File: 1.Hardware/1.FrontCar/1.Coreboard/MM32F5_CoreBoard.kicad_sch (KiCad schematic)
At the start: 61 parts

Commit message: 增加CAN接口
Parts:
- added J? (x2): (no value), symbol Connector_Generic_MountingPin:Conn_01x02_MountingPin
- added R?: 0R, ErBW_s:R_0402, symbol Device:R_Small
- added R?: (no value), ErBW_s:R_0402, symbol Device:R_Small
- added SW? (x3): 3x4, ErBW_s:BUTTON_3x4, symbol Switch:SW_Push
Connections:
- net +3.3VA: now also R?.1; no longer C?.1, C?.1, C?.1, C?.1, C?.2, C?.2, C?.2, C?.2, C?.2, C?.2, C?.2, C?.2, C?.2, C?.2, C?.2, C?.2, C?.2, J?.1 (Pin_1), J?.10 (VCC), J?.12 (LEDA), R?.1, R?.1, R?.1, R?.1, R?.1, U?.108 (VDD), U?.121 (VDD), U?.13 (VDD), U?.131 (VDD), U?.144 (VDD), U?.17 (VDD), U?.3 (VCC), U?.3 (VCC), U?.39 (VDD), U?.5 (VOUT), U?.52 (VDD), U?.6 (VBAT), U?.62 (VDD), U?.72 (VDD), U?.8 (VDDIO), U?.84 (VDD), U?.95 (VDD)
- net CAN1_H: now also J?.2 (Pin_2)
- net CAN1_L: now also J?.1 (Pin_1)
- net CAN2_H: now also J?.2 (Pin_2)
- net CAN2_L: now also J?.1 (Pin_1)
- net ENCODER_A: now also SW?.1
- net ENCODER_B: now also SW?.1
- net GND: now also J?.MP (MountPin), J?.MP (MountPin), R?.2, SW?.2, SW?.2, SW?.2; no longer C?.1, U?.30 (VSSA), U?.31 (VREF-)
- net PG8 renamed KEY_CENTER
- net KEY_CENTER: now also SW?.1
- new net +3.3V: C?.1, C?.1, C?.1, C?.1, C?.2, C?.2, C?.2, C?.2, C?.2, C?.2, C?.2, C?.2, C?.2, C?.2, C?.2, C?.2, C?.2, J?.1 (Pin_1), J?.10 (VCC), J?.12 (LEDA), R?.1, R?.1, R?.1, R?.1, R?.1, R?.2, U?.108 (VDD), U?.121 (VDD), U?.13 (VDD), U?.131 (VDD), U?.144 (VDD), U?.17 (VDD), U?.3 (VCC), U?.3 (VCC), U?.39 (VDD), U?.5 (VOUT), U?.52 (VDD), U?.6 (VBAT), U?.62 (VDD), U?.72 (VDD), U?.8 (VDDIO), U?.84 (VDD), U?.95 (VDD)
- new net GNDA: C?.1, R?.1, U?.30 (VSSA), U?.31 (VREF-)
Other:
- note added: "BTB"
- note added: "KEY"
- note added: "PORTS"
- note removed: "SWD"
- moved on the sheet: C?, D?, J?, R?, U?

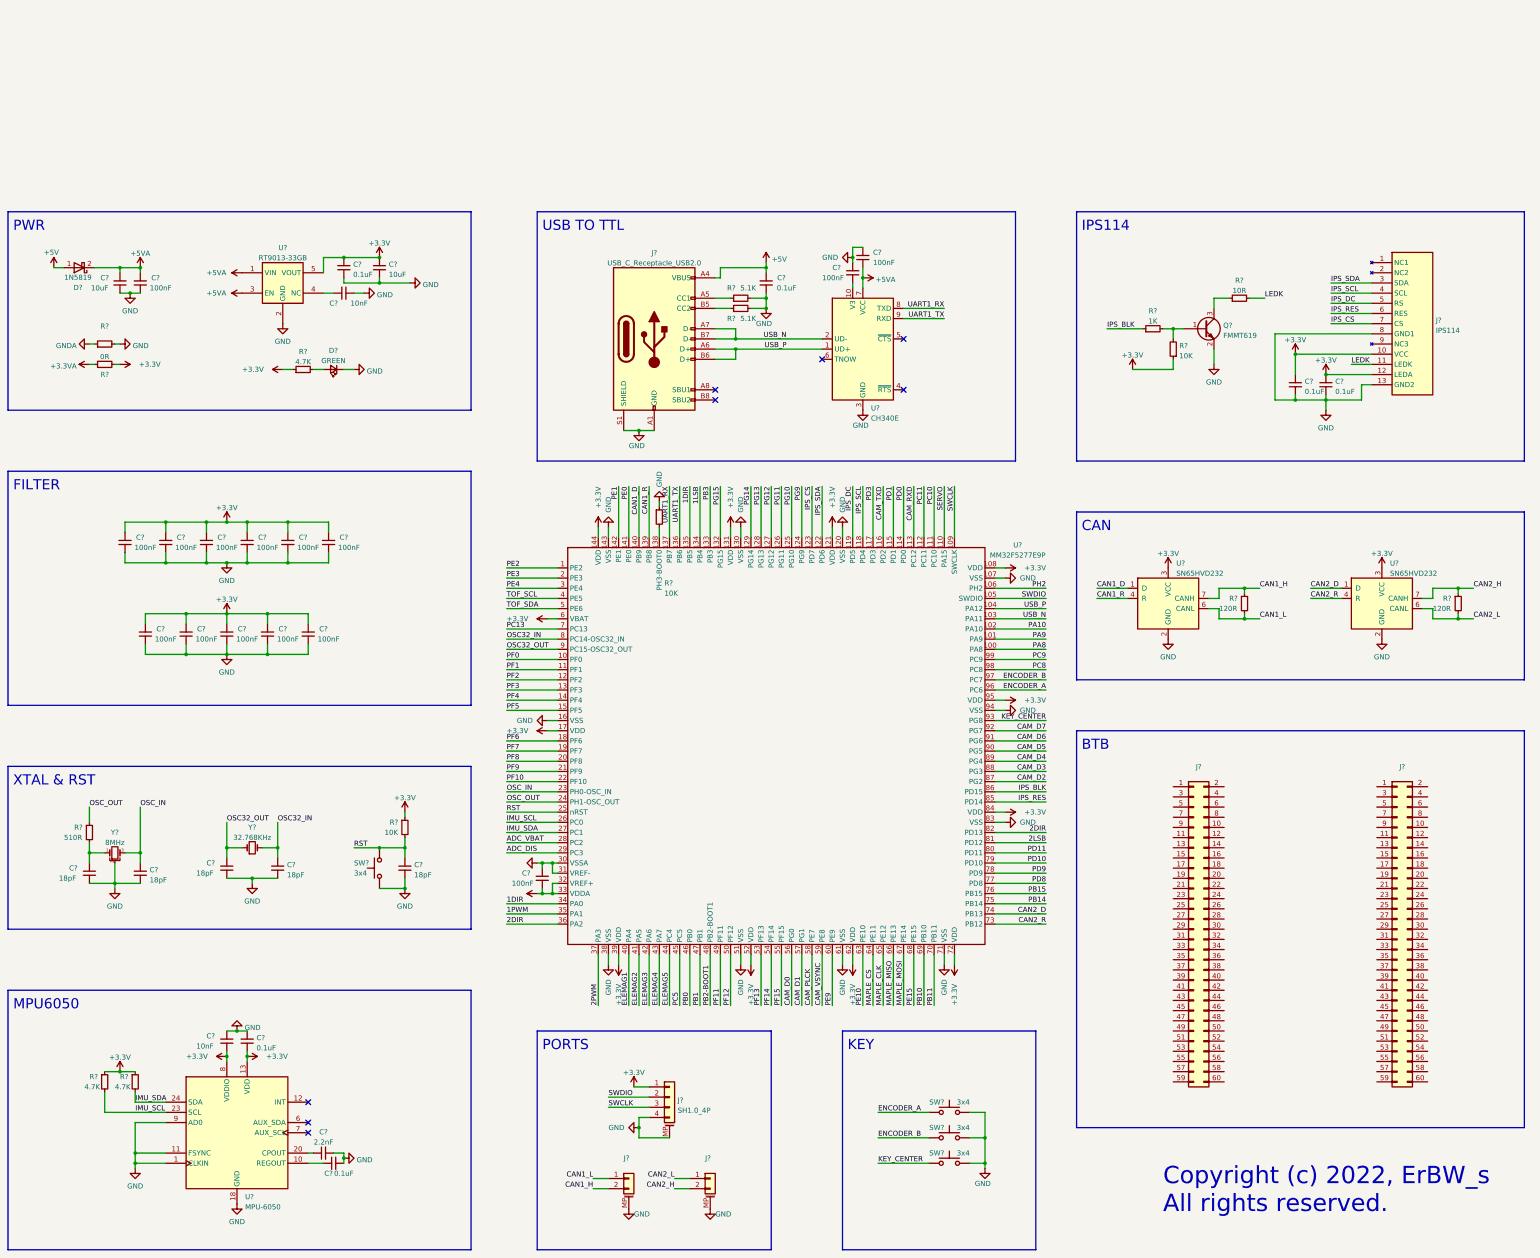
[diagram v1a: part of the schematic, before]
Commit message: 改用ch343p作为usb to ttl 芯片
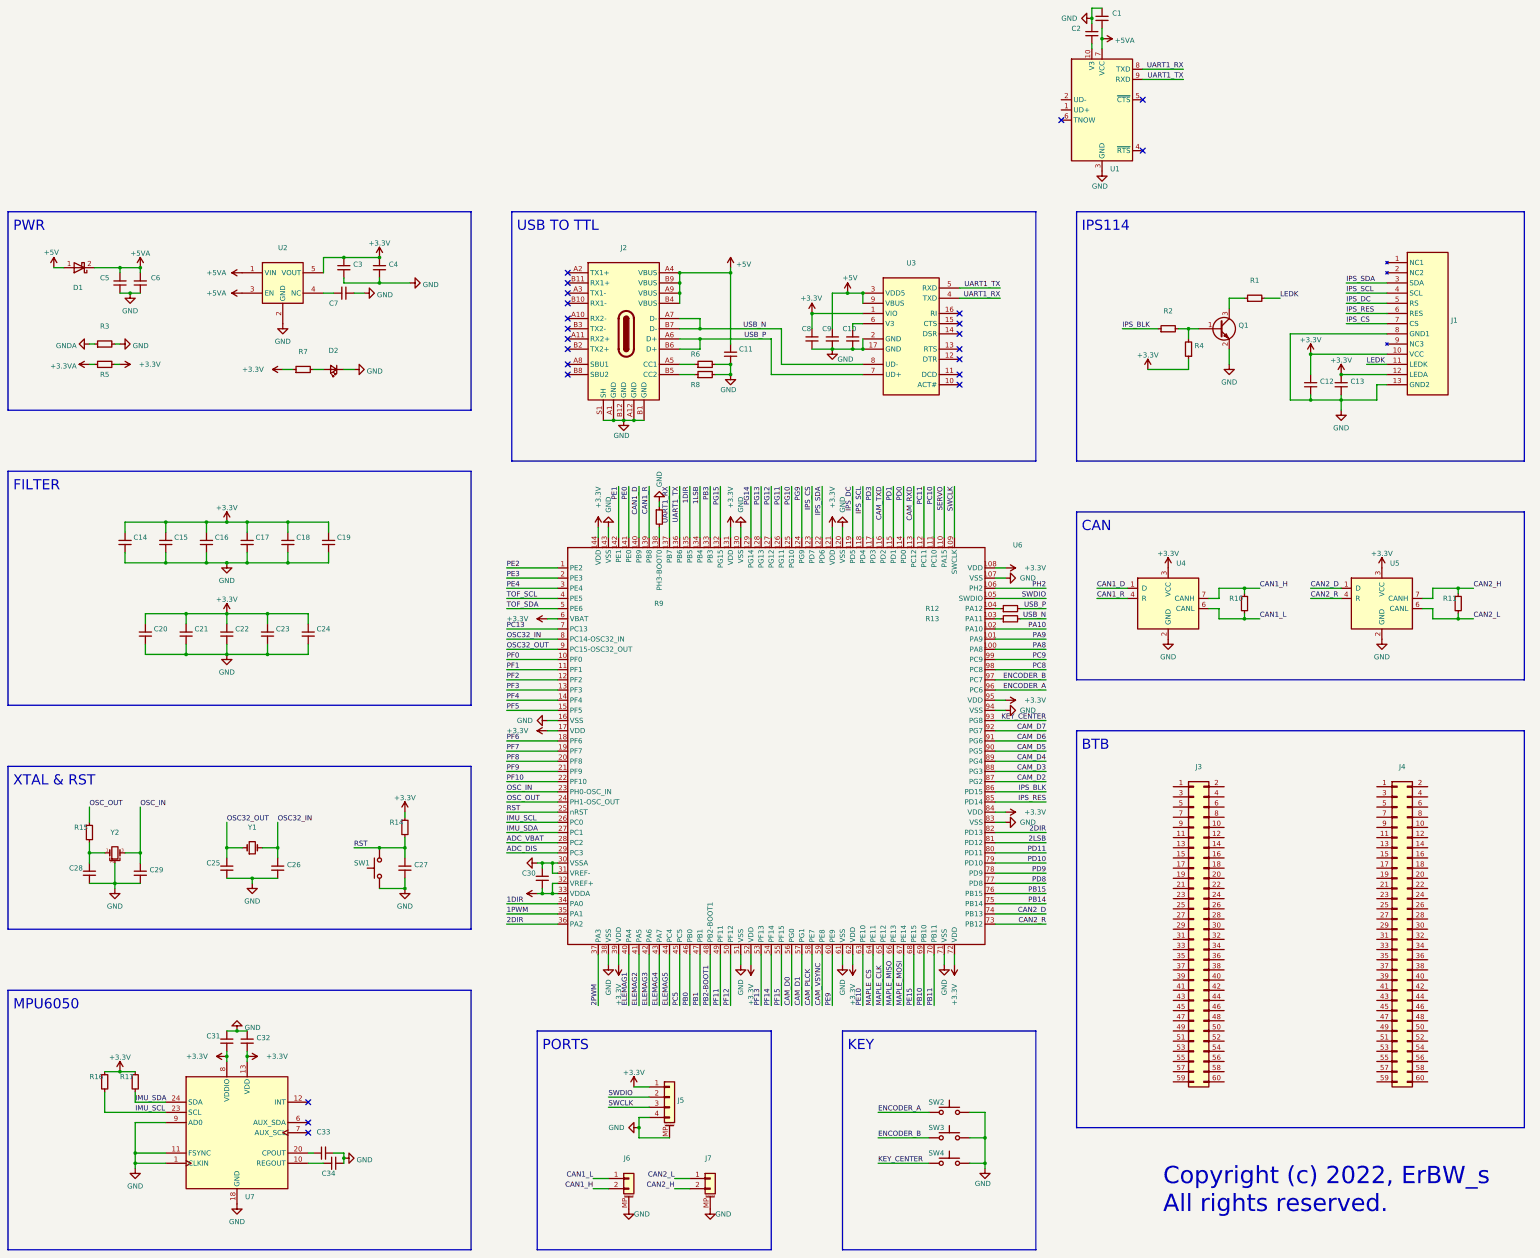
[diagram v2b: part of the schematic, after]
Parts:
- removed C?: 0.1uF, ErBW_s:C_0402, symbol Device:C_Small
- removed J?: USB_C_Receptacle_USB2.0, symbol Connector:USB_C_Receptacle_USB2.0
- removed R? (x2): 5.1K, ErBW_s:R_0402, symbol Device:R_Small
- added C10, C11, C8, C9: (no value), symbol Device:C_Small
- added J2: USB-Type-C, ErBW_s:USB-Type-C_SMD_16P, symbol ErBW_s:USB-Type-C
- added R12, R13, R6, R8: (no value), symbol Device:R_Small
- added U3: CH343P, Package_DFN_QFN:QFN-16-1EP_3x3mm_P0.5mm_EP1.7x1.7mm, symbol ErBW_s:CH343P
- C1, C14, C15, C16, C17, C18, C19, C2, C20, C21, C22, C23, C24, C30, C6: renamed from C?; value 100nF -> (none); footprint ErBW_s:C_0402 -> (none)
- C12, C13, C3, C32, C34: renamed from C?; value 0.1uF -> (none); footprint ErBW_s:C_0402 -> (none)
- C25, C26, C27, C28, C29: renamed from C?; value 18pF -> (none); footprint ErBW_s:C_0402 -> (none)
- C31, C7: renamed from C?; value 10nF -> (none); footprint ErBW_s:C_0402 -> (none)
- C33: renamed from C?; value 2.2nF -> (none); footprint ErBW_s:C_0402 -> (none)
- C4, C5: renamed from C?; value 10uF -> (none); footprint ErBW_s:C_0402 -> (none)
- D1: renamed from D?; value 1N5819 -> (none); footprint ErBW_s:SOD-323 -> (none)
- D2: renamed from D?; value GREEN -> (none); footprint ErBW_s:LED_0402 -> (none)
- J1: renamed from J?; value IPS114 -> (none); footprint ErBW_s:IPS114 -> (none)
- J5: renamed from J?; value SH1.0_4P -> (none); footprint Connector_JST:JST_SH_SM04B-SRSS-TB_1x04-1MP_P1.00mm_Horizontal -> (none)
- J6: renamed from J?; value (none) -> SH1.0_2P; footprint (none) -> Connector_JST:JST_SH_SM02B-SRSS-TB_1x02-1MP_P1.00mm_Horizontal
- Q1: renamed from Q?; value FMMT619 -> (none); footprint Package_TO_SOT_SMD:SOT-23 -> (none)
- R1: renamed from R?; value 10R -> (none); footprint ErBW_s:R_0402 -> (none)
- R10, R11: renamed from R?; value 120R -> (none); footprint ErBW_s:R_0402 -> (none)
- R14, R4, R9: renamed from R?; value 10K -> (none); footprint ErBW_s:R_0402 -> (none)
- R15: renamed from R?; value 510R -> (none); footprint ErBW_s:R_0402 -> (none)
- R16, R17, R7: renamed from R?; value 4.7K -> (none); footprint ErBW_s:R_0402 -> (none)
- R2: renamed from R?; value 1K -> (none); footprint ErBW_s:R_0402 -> (none)
- R3: renamed from R?; footprint ErBW_s:R_0402 -> (none)
- R5: renamed from R?; value 0R -> (none); footprint ErBW_s:R_0402 -> (none)
- SW1, SW2, SW3, SW4: renamed from SW?; value 3x4 -> (none); footprint ErBW_s:BUTTON_3x4 -> (none)
- U1: renamed from U?; value CH340E -> (none); footprint Package_SO:MSOP-10_3x3mm_P0.5mm -> (none)
- U2: renamed from U?; value RT9013-33GB -> (none); footprint Package_TO_SOT_SMD:SOT-23-5 -> (none)
- U4, U5: renamed from U?; value SN65HVD232 -> (none); footprint Package_SO:SOIC-8_3.9x4.9mm_P1.27mm -> (none)
- U6: renamed from U?; value MM32F5277E9P -> (none); footprint Package_QFP:LQFP-144_20x20mm_P0.5mm -> (none)
- U7: renamed from U?; value MPU-6050 -> (none); footprint Sensor_Motion:InvenSense_QFN-24_4x4mm_P0.5mm -> (none)
- Y1: renamed from Y?; value 32.768KHz -> (none); footprint ErBW_s:Crystal_SMD_3215_FC-135_2P -> (none)
- Y2: renamed from Y?; value 8MHz -> (none); footprint ErBW_s:Crystal_SMD_3213_3P -> (none)
- gave numbers to parts that had none: 3
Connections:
- net +3.3V: now also C8.1, U3.1 (VIO)
- net +5V: now also C11.2, C9.1, J2.A4 (VBUS), J2.A9 (VBUS), J2.B4 (VBUS), J2.B9 (VBUS), U3.3 (VDD5), U3.9 (VBUS)
- net GND: now also C10.2, C11.1, C8.2, C9.2, J2.A1 (GND), J2.A12 (GND), J2.B1 (GND), J2.B12 (GND), J2.S1 (SH), R6.2, R8.2, U3.17 (GND), U3.2 (GND)
- net UART1_RX: now also U3.4 (TXD)
- net UART1_TX: now also U3.5 (RXD)
- net USB_N: now also J2.A7 (D-), J2.B7 (D-), R13.2, U3.8 (UD-); no longer U1.2 (UD-), U6.103 (PA11)
- net USB_P: now also J2.A6 (D+), J2.B6 (D+), R12.2, U3.7 (UD+); no longer U1.1 (UD+), U6.104 (PA12)
- new net: R13.1, U6.103 (PA11)
- new net: R12.1, U6.104 (PA12)
- new net: C10.1, U3.6 (V3)
- new net: J2.A5 (CC1), R6.1
- new net: J2.B5 (CC2), R8.1
- no-connect marks 8 -> 23
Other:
- moved on the sheet: C1, C12, C13, C2, J1, Q1, R1, R2, R4, U1
